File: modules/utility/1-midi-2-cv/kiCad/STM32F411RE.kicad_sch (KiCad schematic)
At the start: 20 parts, among them J5 BOOT_RUN, J6 Conn_01x04, U11 STM32F411RETx, Y2 20MHZ

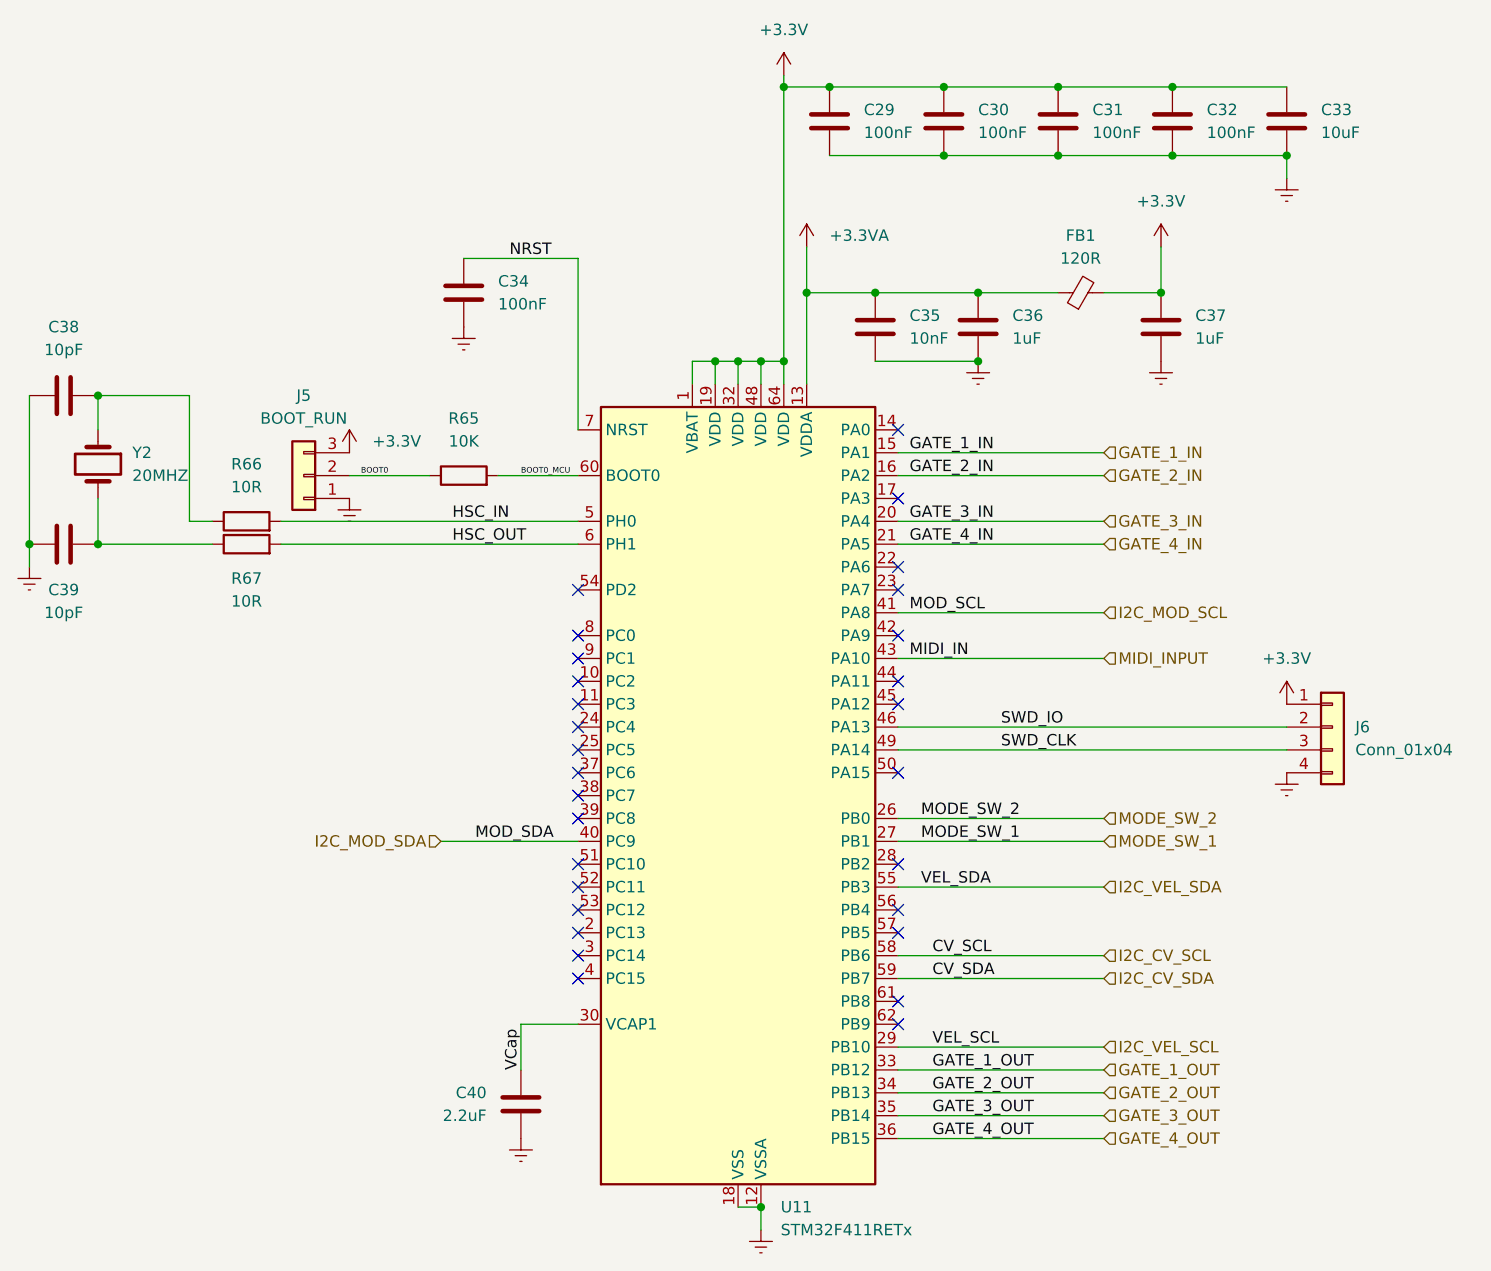
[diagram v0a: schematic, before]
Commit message: debugging and rework for ricochet, midas, wolkje. Added IBOM for drums and other modules.
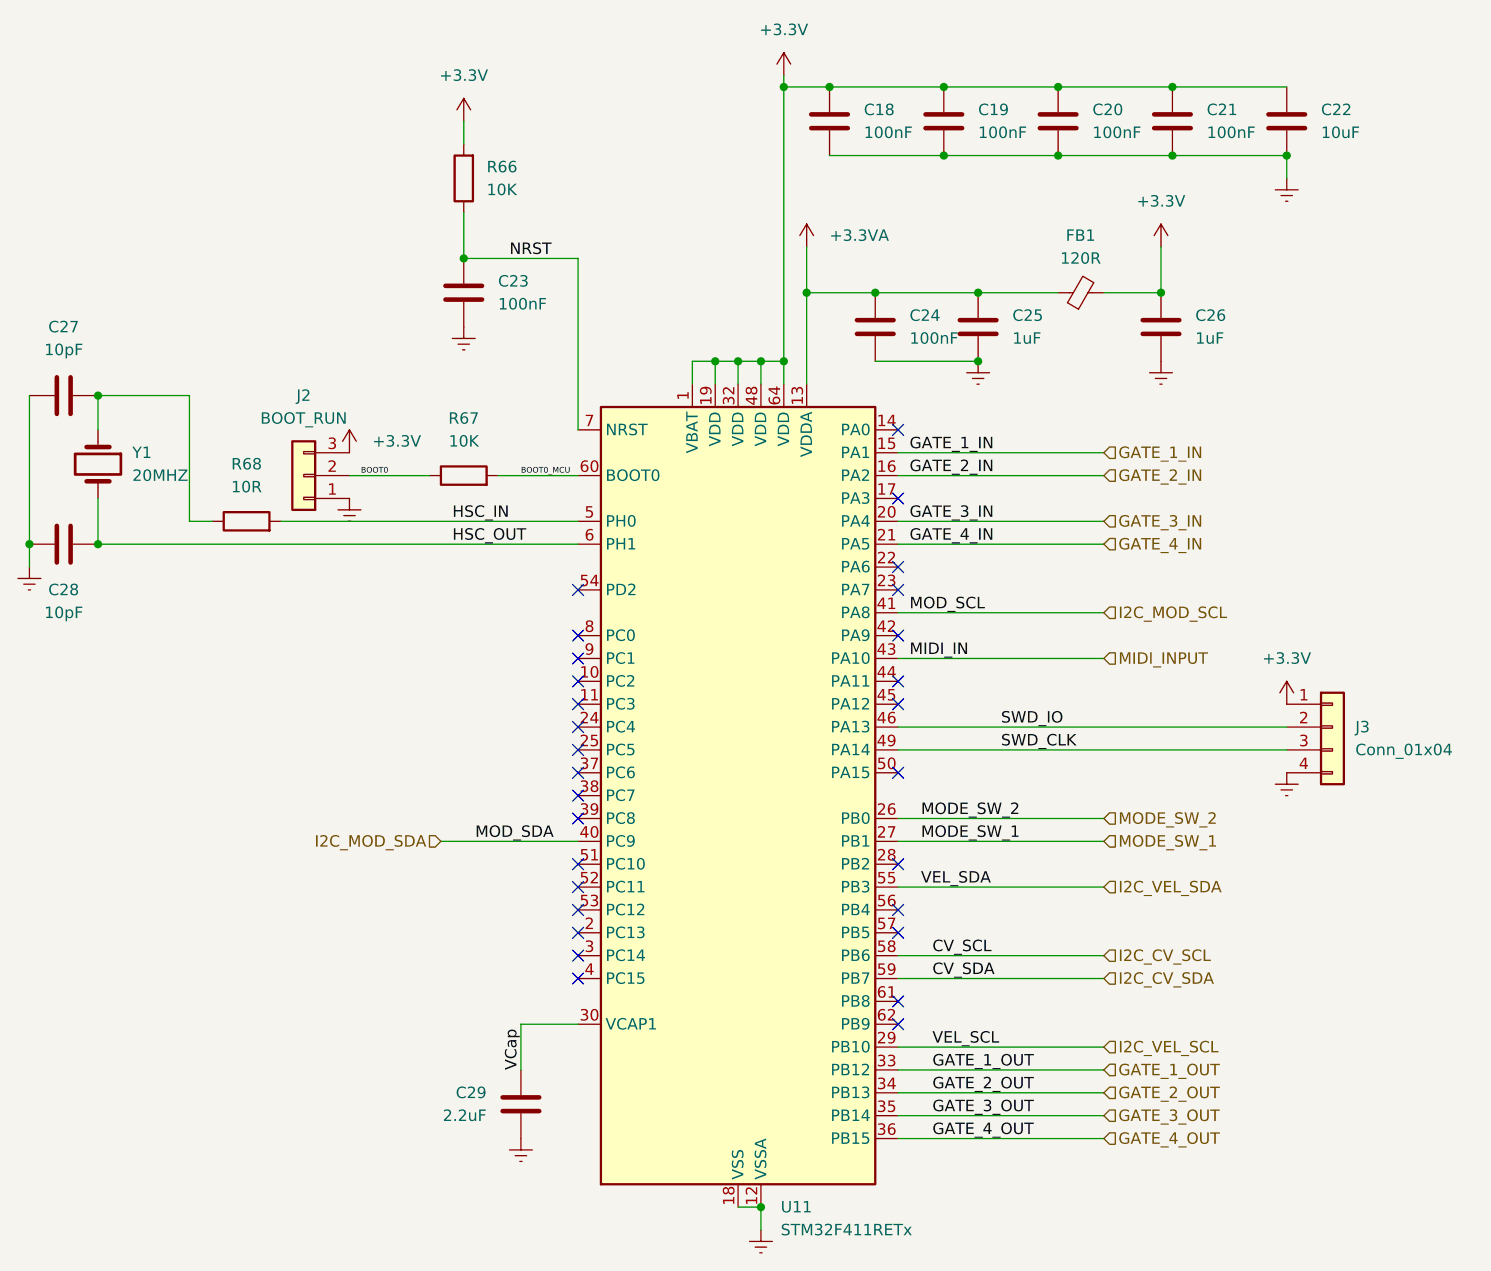
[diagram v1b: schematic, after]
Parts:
- removed R67: 10R, Resistor_SMD:R_0805_2012Metric_Pad1.20x1.40mm_HandSolder, symbol Device:R
- added R66: 10K, Resistor_SMD:R_0805_2012Metric_Pad1.20x1.40mm_HandSolder, symbol Device:R
- C24: renamed from C35; value 10nF -> 100nF
- renumbered C29 to C18, C30 to C19, C31 to C20, C32 to C21, C33 to C22, C34 to C23, C36 to C25, C37 to C26, C38 to C27, C39 to C28, C40 to C29, J5 to J2, J6 to J3, R65 to R67, R66 to R68, Y2 to Y1
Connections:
- net +3.3V: now also R66.2
- net HSC_OUT: now also C28.1, Y1.2
- net NRST: now also R66.1

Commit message: Preperation for Run3, wolkje, ricochet readme and final exports
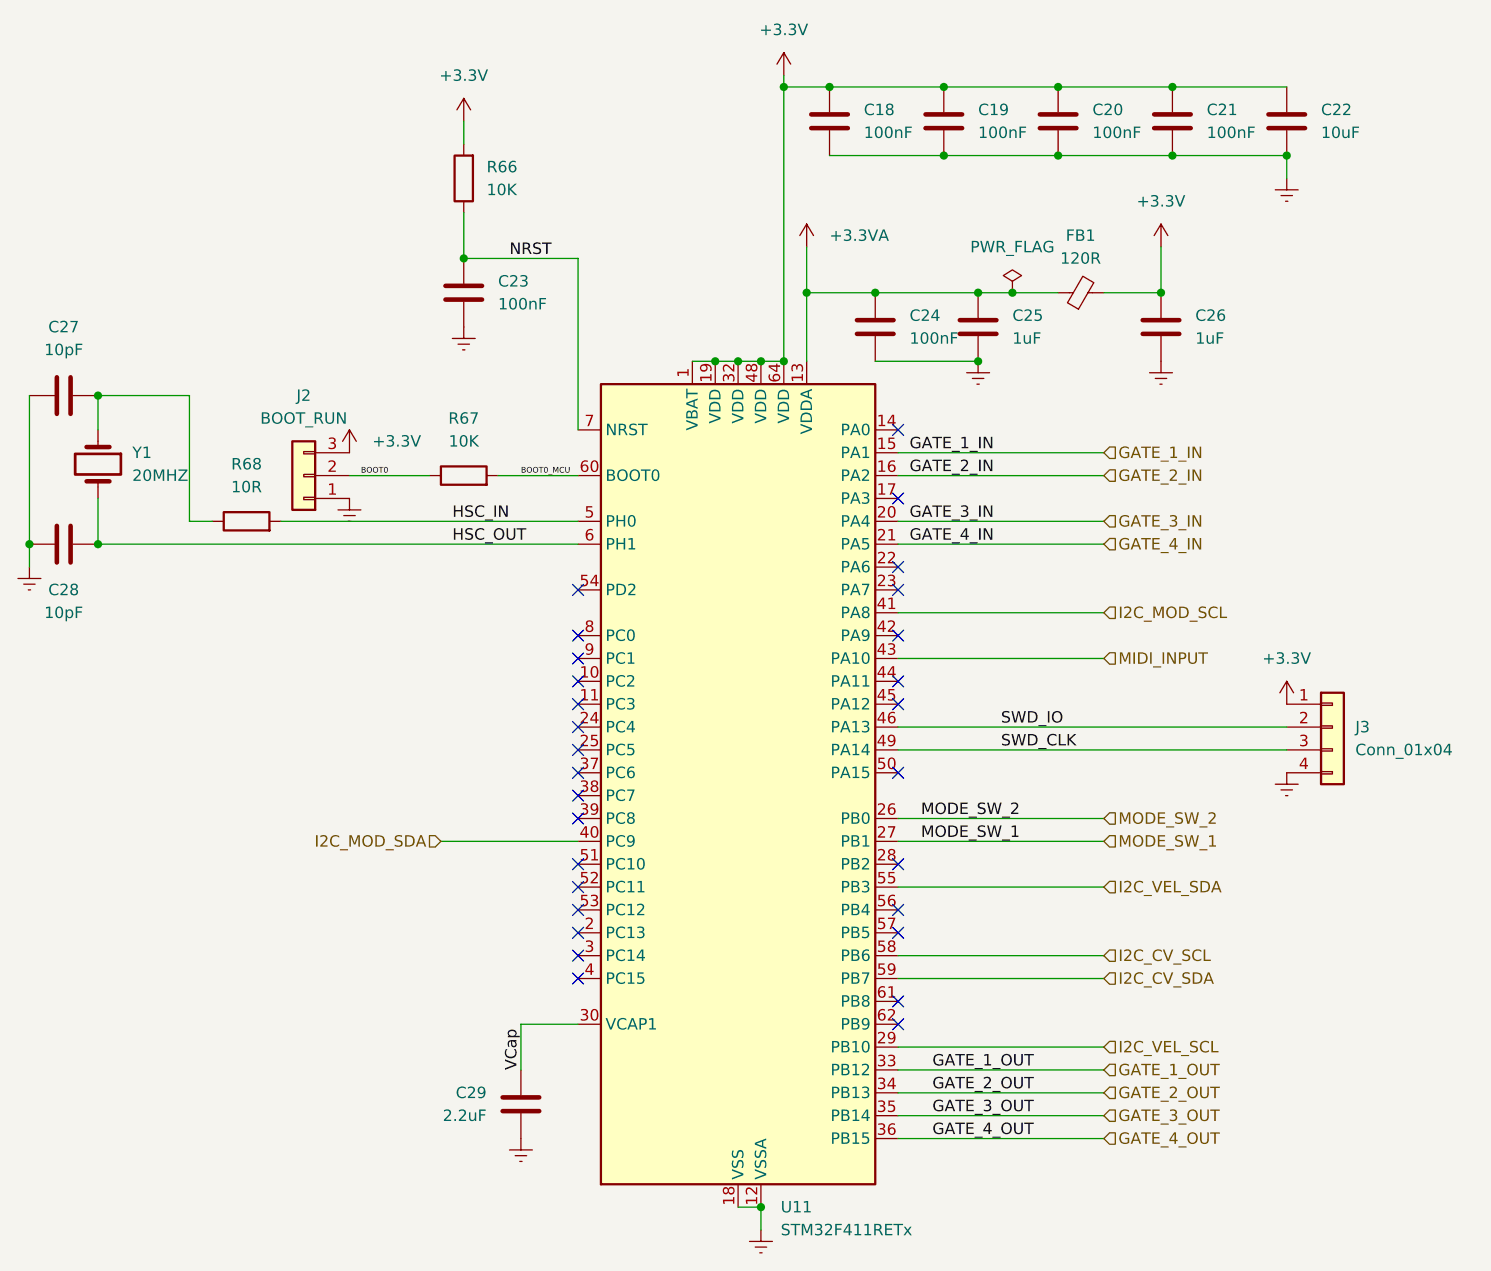
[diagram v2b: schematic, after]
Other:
- moved on the sheet: U11
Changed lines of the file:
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@@
 	)
 	(junction
-		(at 198.12 95.25)
+		(at 129.54 115.57)
 		(diameter 0)
 		(color 0 0 0 0)
 	)
 	(junction
-		(at 129.54 115.57)
+		(at 205.74 95.25)
 		(diameter 0)
 		(color 0 0 0 0)
@@
 	)
 	(junction
+		(at 208.28 87.63)
+		(diameter 0)
+		(color 0 0 0 0)
+	)
+	(junction
 		(at 248.92 72.39)
 		(diameter 0)
@@
 	)
 	(junction
+		(at 231.14 87.63)
+		(diameter 0)
+		(color 0 0 0 0)
+	)
+	(junction
 		(at 205.74 64.77)
 		(diameter 0)
@@
 	)
 	(junction
-		(at 236.22 64.77)
+		(at 198.12 95.25)
 		(diameter 0)
 		(color 0 0 0 0)
 	)
 	(junction
-		(at 129.54 99.06)
+		(at 236.22 64.77)
 		(diameter 0)
 		(color 0 0 0 0)
 	)
 	(junction
-		(at 208.28 87.63)
+		(at 129.54 99.06)
 		(diameter 0)
 		(color 0 0 0 0)
@@
 	)
 	(junction
-		(at 205.74 95.25)
+		(at 203.2 95.25)
 		(diameter 0)
 		(color 0 0 0 0)
@@
 	)
 	(junction
-		(at 200.66 95.25)
-		(diameter 0)
-		(color 0 0 0 0)
-	)
-	(junction
 		(at 121.92 115.57)
 		(diameter 0)
@@
 	)
 	(junction
-		(at 203.2 95.25)
+		(at 261.62 72.39)
 		(diameter 0)
 		(color 0 0 0 0)
 	)
 	(junction
-		(at 261.62 72.39)
+		(at 200.66 95.25)
 		(diameter 0)
 		(color 0 0 0 0)
@@
 	(wire
 		(pts
-			(xy 205.74 64.77) (xy 205.74 95.25)
-		)
-		(stroke
-			(width 0)
-			(type default)
-		)
-	)
-	(wire
-		(pts
-			(xy 227.33 87.63) (xy 236.22 87.63)
-		)
-		(stroke
-			(width 0)
-			(type default)
-		)
-	)
-	(wire
-		(pts
-			(xy 215.9 87.63) (xy 227.33 87.63)
+			(xy 200.66 95.25) (xy 203.2 95.25)
 		)
 		(stroke
@@
 	(wire
 		(pts
-			(xy 248.92 72.39) (xy 261.62 72.39)
+			(xy 205.74 64.77) (xy 205.74 95.25)
 		)
 		(stroke
@@
 	(wire
 		(pts
-			(xy 218.44 105.41) (xy 241.3 105.41)
+			(xy 227.33 87.63) (xy 231.14 87.63)
 		)
 		(stroke
@@
 	(wire
 		(pts
-			(xy 223.52 64.77) (xy 236.22 64.77)
+			(xy 215.9 87.63) (xy 227.33 87.63)
 		)
 		(stroke
@@
 	(wire
 		(pts
-			(xy 200.66 95.25) (xy 200.66 97.79)
+			(xy 248.92 72.39) (xy 261.62 72.39)
 		)
 		(stroke
@@
 	(wire
 		(pts
-			(xy 205.74 95.25) (xy 205.74 97.79)
+			(xy 218.44 105.41) (xy 241.3 105.41)
 		)
 		(stroke
@@
 	(wire
 		(pts
-			(xy 203.2 95.25) (xy 203.2 97.79)
+			(xy 223.52 64.77) (xy 236.22 64.77)
 		)
 		(stroke
@@
 	(wire
 		(pts
-			(xy 200.66 95.25) (xy 203.2 95.25)
+			(xy 195.58 95.25) (xy 198.12 95.25)
 		)
 		(stroke
@@
 	(wire
 		(pts
-			(xy 218.44 135.89) (xy 261.62 135.89)
+			(xy 198.12 95.25) (xy 200.66 95.25)
 		)
 		(stroke
@@
 	(wire
 		(pts
-			(xy 198.12 95.25) (xy 195.58 95.25)
+			(xy 218.44 135.89) (xy 261.62 135.89)
 		)
 		(stroke
@@
 	(wire
 		(pts
-			(xy 241.3 163.83) (xy 218.44 163.83)
+			(xy 208.28 87.63) (xy 208.28 95.25)
 		)
 		(stroke
@@
 	(wire
 		(pts
-			(xy 198.12 95.25) (xy 200.66 95.25)
+			(xy 241.3 163.83) (xy 218.44 163.83)
 		)
 		(stroke
@@
 	(wire
 		(pts
-			(xy 223.52 72.39) (xy 236.22 72.39)
+			(xy 203.2 95.25) (xy 205.74 95.25)
 		)
 		(stroke
@@
 	(wire
 		(pts
-			(xy 121.92 115.57) (xy 121.92 118.11)
+			(xy 223.52 72.39) (xy 236.22 72.39)
 		)
 		(stroke
@@
 	(wire
 		(pts
-			(xy 203.2 95.25) (xy 205.74 95.25)
+			(xy 121.92 115.57) (xy 121.92 118.11)
 		)
 		(stroke
@@
 	(wire
 		(pts
-			(xy 198.12 97.79) (xy 198.12 95.25)
-		)
-		(stroke
-			(width 0)
-			(type default)
-		)
-	)
-	(wire
-		(pts
 			(xy 129.54 110.49) (xy 129.54 115.57)
 		)
@@
 	(wire
 		(pts
-			(xy 218.44 181.61) (xy 241.3 181.61)
+			(xy 231.14 87.63) (xy 236.22 87.63)
 		)
 		(stroke
@@
 	(wire
 		(pts
-			(xy 195.58 95.25) (xy 195.58 97.79)
+			(xy 218.44 181.61) (xy 241.3 181.61)
 		)
 		(stroke
@@
 		)
 	)
-	(wire
-		(pts
-			(xy 208.28 97.79) (xy 208.28 87.63)
-		)
-		(stroke
-			(width 0)
-			(type default)
-		)
-	)
-	(label "CV_SDA"
-		(at 222.25 163.83 0)
-		(effects
-			(font
-				(size 1.27 1.27)
-			)
-			(justify left bottom)
-		)
-	)
 	(label "GATE_3_OUT"
 		(at 222.25 179.07 0)
@@
 		)
 	)
-	(label "CV_SCL"
-		(at 222.25 161.29 0)
-		(effects
-			(font
-				(size 1.27 1.27)
-			)
-			(justify left bottom)
-		)
-	)
 	(label "SWD_IO"
 		(at 229.87 135.89 0)
@@
 		)
 	)
-	(label "VEL_SCL"
-		(at 222.25 171.45 0)
-		(effects
-			(font
-				(size 1.27 1.27)
-			)
-			(justify left bottom)
-		)
-	)
-	(label "MIDI_IN"
-		(at 219.71 128.27 0)
-		(effects
-			(font
-				(size 1.27 1.27)
-			)
-			(justify left bottom)
-		)
-	)
-	(label "MOD_SCL"
-		(at 219.71 123.19 0)
-		(effects
-			(font
-				(size 1.27 1.27)
-			)
-			(justify left bottom)
-		)
-	)
 	(label "HSC_IN"
 		(at 168.91 113.03 0)
@@
 		)
 	)
-	(label "MOD_SDA"
-		(at 171.45 148.59 0)
-		(effects
-			(font
-				(size 1.27 1.27)
-			)
-			(justify left bottom)
-		)
-	)
 	(label "NRST"
 		(at 175.26 83.82 0)
@@
 		)
 	)
-	(label "VEL_SDA"
-		(at 220.98 153.67 0)
-		(effects
-			(font
-				(size 1.27 1.27)
-			)
-			(justify left bottom)
-		)
-	)
 	(label "MODE_SW_2"
 		(at 220.98 146.05 0)
@@
 					(unit 1)
 				)
+			)
+		)
+	)
+	(symbol
+		(lib_id "power:PWR_FLAG")
+		(at 231.14 87.63 0)
+		(unit 1)
+		(exclude_from_sim no)
+		(in_bom yes)
+		(on_board yes)
+		(dnp no)
+		(fields_autoplaced yes)
+		(property "Reference" "#FLG05"
+			(at 231.14 85.725 0)
+			(effects
+				(font
+					(size 1.27 1.27)
+				)
+				(hide yes)
+			)
+		)
+		(property "Value" "PWR_FLAG"
+			(at 231.14 82.55 0)
+			(effects
+				(font
+					(size 1.27 1.27)
+				)
+			)
+		)
+		(property "Footprint" ""
+			(at 231.14 87.63 0)
+			(effects
+				(font
+					(size 1.27 1.27)
+				)
+				(hide yes)
+			)
+		)
+		(property "Datasheet" "~"
+			(at 231.14 87.63 0)
+			(effects
+				(font
+					(size 1.27 1.27)
+				)
+				(hide yes)
+			)
+		)
+		(property "Description" "Special symbol for telling ERC where power comes from"
+			(at 231.14 87.63 0)
+			(effects
+				(font
+					(size 1.27 1.27)
+				)
+				(hide yes)
+			)
+		)
+		(pin "1"
+		)
+		(instances
+			(project ""
+				(path "/ffcc7acb-943e-4c85-833d-d9691a289ebb/397e51e1-d2d3-448e-96ce-70aea9e0c68a"
+					(reference "#FLG05")
+					(unit 1)
+				)
